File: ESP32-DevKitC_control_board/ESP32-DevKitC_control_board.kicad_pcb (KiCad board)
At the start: 2 copper layers, 100 x 100 mm, 35 parts, among them J1 Conn_01x03_Pin, J10 Conn_01x02_Pin, J11 Conn_01x02_Pin, J2 Conn_01x03_Pin, J3 Conn_01x02_Pin, J4 Conn_01x02_Pin, J5 Conn_01x04_Pin, J6 Conn_01x03_Pin, J7 Conn_01x03_Pin, J8 Conn_01x03_Pin, J9 Conn_01x03_Pin, U1 ESP32-DevKitC, U2 MCP2562-E-P

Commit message: ESP32基板　基板完成，ver 0.1
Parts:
- added D4: LED, LED_THT:LED_D5.0mm, F.Cu at (90.7, 33.0)
- added R12: 1k, Resistor_THT:R_Axial_DIN0207_L6.3mm_D2.5mm_P2.54mm_Vertical, F.Cu at (93.0, 24.4)
- C2: renamed from C1; footprint Capacitor_THT:C_Disc_D4.3mm_W1.9mm_P5.00mm -> Capacitor_THT:C_Disc_D5.0mm_W2.5mm_P2.50mm
- C3: renamed from C2; footprint Capacitor_THT:C_Disc_D4.3mm_W1.9mm_P5.00mm -> Capacitor_THT:C_Disc_D5.0mm_W2.5mm_P2.50mm
- J7: renamed from J5; footprint OU_connector:DF1EC-4P-2.5DSA -> OU_connector:DF1E-4P-2.5DS
- R1: footprint Resistor_THT:R_Axial_DIN0204_L3.6mm_D1.6mm_P5.08mm_Horizontal -> Resistor_THT:R_Axial_DIN0207_L6.3mm_D2.5mm_P2.54mm_Vertical
- moved J9 156.3 mm to (36.8, 68.8), turned to -90 degrees
- moved J5 152.9 mm to (48.3, 49.8), turned to 180 degrees
- moved C5 151.7 mm to (45.7, 71.6), turned to -90 degrees
- moved C3 150.5 mm to (49.5, 32.0), turned to 180 degrees
- moved J4 146.6 mm to (40.9, 44.7), turned to 90 degrees
- moved C2 145.8 mm to (53.1, 32.0)
- moved J7 141.6 mm to (40.9, 61.9), turned to 90 degrees
- moved U1 131.9 mm to (54.6, 42.9), turned to 180 degrees
- moved J6 128.5 mm to (40.9, 33.5), turned to 90 degrees
- moved R5 127.2 mm to (45.7, 68.8), turned to 90 degrees
- moved R9 126.4 mm to (41.4, 71.4), turned to 90 degrees
- moved R1 121.4 mm to (52.1, 49.8), turned to 90 degrees
- moved R2 120.1 mm to (47.5, 56.9), turned to 90 degrees
- moved R3 120.0 mm to (47.5, 62.2), turned to 90 degrees
- moved C1 115.7 mm to (87.9, 22.6), turned to -90 degrees
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- renumbered C7 to C1, C3 to C4, C4 to C5, C5 to C7, J10 to J1, J7 to J10, J6 to J11, J1 to J2, J2 to J3, J11 to J4, J3 to J5, J4 to J6, R22 to R10, R20 to R11, R14 to R2, R15 to R3, R17 to R4, R19 to R5, R23 to R6, R21 to R7, R16 to R8, R18 to R9, U2 to U1, U1 to U2
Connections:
- J3 pad 1: /PWM2 -> /PWM3
- J3 pad 3: /PWM3 -> /PWM2
- J7 pad 2: /GPIO27 -> /GPIO22
- J7 pad 4: /GPIO26 -> /GPIO21
- R2 pad 2: /GPIO26 -> /GPIO21
- R3 pad 2: /GPIO27 -> /GPIO22
- R9 pad 1: /GPIO14 -> /GPIO23
- U2 pad 10: /GPIO26 -> /PWM3
- U2 pad 11: /GPIO27 -> /PWM1
- U2 pad 12: /GPIO14 -> /PWM0
- U2 pad 30: /PWM1 -> /CAN_RX
- U2 pad 31: /PWM0 -> /CAN_TX
- U2 pad 33: /CAN_RX -> /GPIO21
- U2 pad 36: /CAN_TX -> /GPIO22
- U2 pad 37: /PWM2 -> /GPIO23
- U2 pad 9: /PWM3 -> /PWM2
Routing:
- net +3.3V: track 0.00 -> 230.4 mm
- net +5V: track 0.00 -> 67.0 mm
- net /GPIO4: track 0.00 -> 32.6 mm
- net /PWM3: track 0.00 -> 32.3 mm
- net /PWM0: track 0.00 -> 27.1 mm
- net /PWM1: track 0.00 -> 26.5 mm
- net /PWM2: track 0.00 -> 25.9 mm
- net /GPIO22: track 0.00 -> 25.6 mm
- net /CAN_RX: track 0.00 -> 25.1 mm
- net /GPIO33: track 0.00 -> 24.0 mm
- net /GPIO21: track 0.00 -> 23.4 mm, vias 0 -> 1
- net Net-(J8-Pin_1): track 0.00 -> 20.9 mm
- net /GPIO23: track 0.00 -> 20.7 mm
- net /GPIO32: track 0.00 -> 20.6 mm
- net /CAN_TX: track 0.00 -> 20.0 mm
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- added copper zone on B.Cu, net GND
- added copper zone on F.Cu, net GND
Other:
- board size 100 x 100 mm -> 85 x 60 mm
- board text added: "3.3V"
- board text added: "5V"
- board text added: "5V INPUT"
- board text added: "5V INPUTと USBを併用しない!"
- board text added: ":"
- board text added: "BoardID: TS26-CTRL-ESP32 ver 0.1"
- board text added: "CAN0"
- board text added: "GND"
- board text added: "GPIO13"
- board text added: "GPIO13,23, 32,33"
- board text added: "GPIO23"
- board text added: "GPIO32"
- board text added: "GPIO33"
- board text added: "GPIO4"
- board text added: "I2C"
- board text added: "IO"
- board text added: "Lp-C P-dn"
- board text added: "Lp-C ローパスフィルタ用C, P-dn もしくはプルダウン"
- board text added: "Lp-R"
- board text added: "Lp-R: ローパスフィルタ用R"
- board text added: "P-up"
- board text added: "P-up: プルアップ"
- board text added: "PW0,2"
- board text added: "PW1,3"
- board text added: "PWM0,1"
- board text added: "PWM2,3"
- board text added: "Pull-up Resistor"
- board text added: "SCL"
- board text added: "SDA"
- board text added: "Serial Servo"
- board text added: "ローパスフィルタ未使用時 Lp-Rは0Ωに"
- board text added: "岡山大学 ロボット研究会"
- board text added: "終端抵抗 有効化"

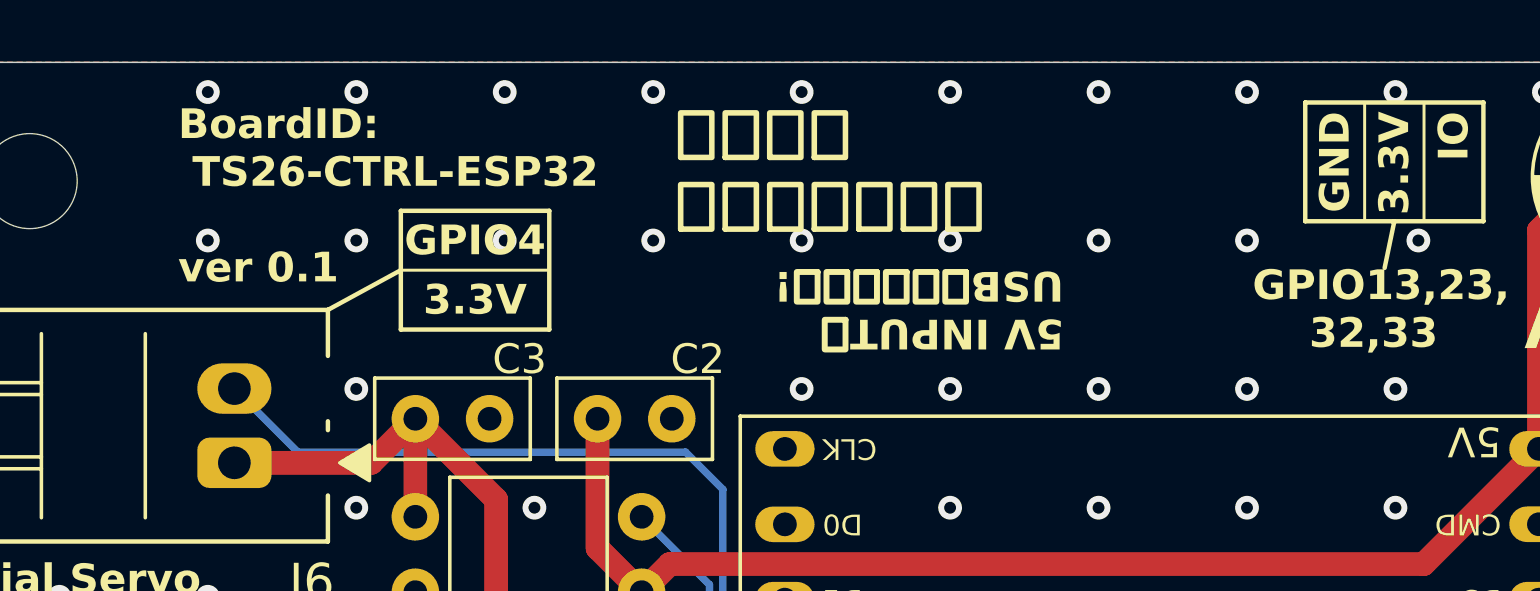
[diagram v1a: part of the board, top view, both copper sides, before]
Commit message: ESP32基板　不足していたシルクを追加
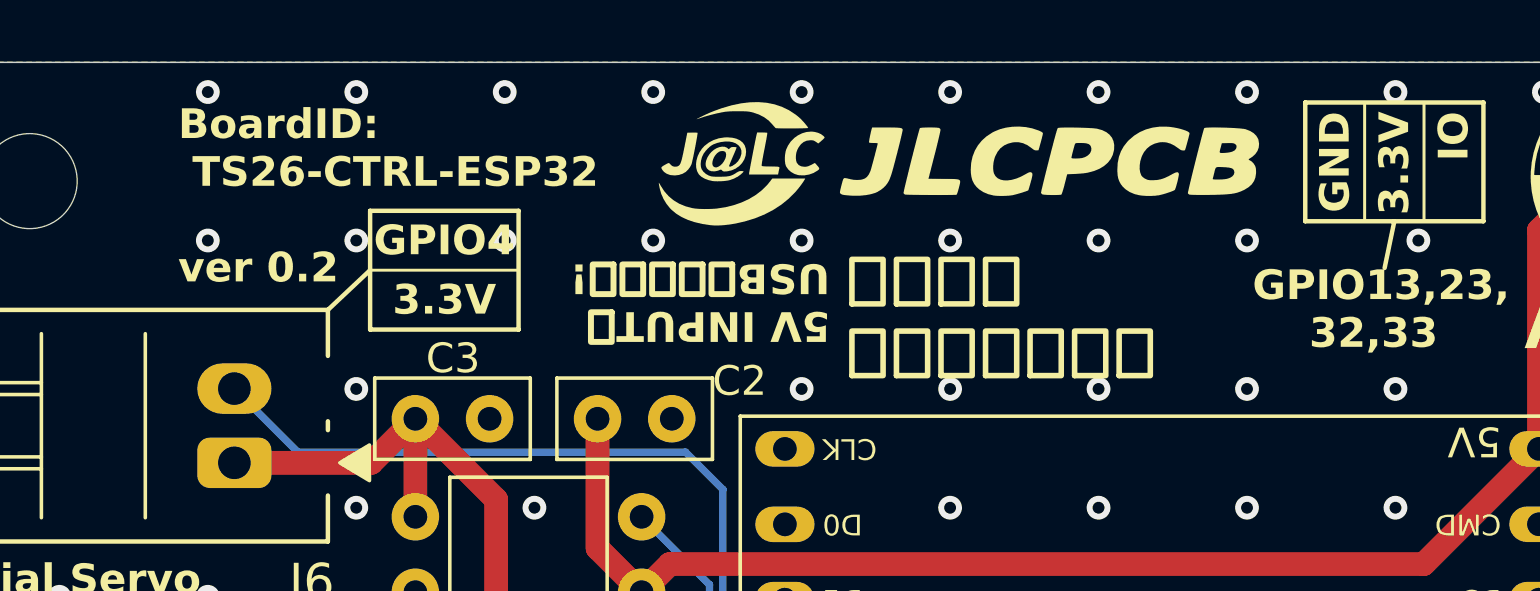
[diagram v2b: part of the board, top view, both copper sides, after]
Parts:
- added G***: LOGO, OU_Picture:JLCPCB_Logo_4x20, F.Cu at (65.3, 23.4)
- added G***: LOGO, OU_Picture:OkaLogo, B.Cu at (72.6, 34.3)
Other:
- board text added: "2026/10/02 Designed by E.Yoshioka"
- board text added: "5V INPUTと USBの併用ダメ!"
- board text added: "BoardID: TS26-CTRL-ESP32 ver 0.2"
- board text added: "No."
- board text removed: "5V INPUTと USBを併用しない!"
- board text removed: "BoardID: TS26-CTRL-ESP32 ver 0.1"

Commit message: ESP32基板　CAN0をCAN1に改名，ver 0.3 STMの場合，CANの通し番号は1からっぽい．
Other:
- board text added: "BoardID: TS26-CTRL-ESP32 ver 0.3"
- board text added: "CAN1"
- board text removed: "BoardID: TS26-CTRL-ESP32 ver 0.2"
- board text removed: "CAN0"
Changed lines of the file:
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@@
 		)
 	)
-	(gr_text "BoardID:\n TS26-CTRL-ESP32\n\nver 0.2"
+	(gr_text "BoardID:\n TS26-CTRL-ESP32\n\nver 0.3"
 		(at 39 24.5 0)
 		(layer "F.SilkS")
@@
 		)
 	)
-	(gr_text "CAN0"
+	(gr_text "CAN1"
 		(at 30.4 49.2 0)
 		(layer "F.SilkS" knockout)

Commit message: ESP32基板　I2C部分のネットラベル名を変更
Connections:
- net /CAN0+ renamed /CAN1+
- net /CAN0- renamed /CAN1-
- net /GPIO21 renamed /I2C_SDA
- net /GPIO22 renamed /I2C_SCL
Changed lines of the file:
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@@
 			(layers "*.Cu" "*.Mask")
 			(remove_unused_layers no)
-			(net "/GPIO21")
+			(net "/I2C_SDA")
 			(pinfunction "GPIO21_33")
 			(pintype "bidirectional")
@@
 			(layers "*.Cu" "*.Mask")
 			(remove_unused_layers no)
-			(net "/GPIO22")
+			(net "/I2C_SCL")
 			(pinfunction "GPIO22_36")
 			(pintype "bidirectional")
@@
 			(layers "*.Cu" "*.Mask")
 			(remove_unused_layers no)
-			(net "/GPIO22")
+			(net "/I2C_SCL")
 			(pinfunction "Pin_2_2")
 			(pintype "passive")
@@
 			(layers "*.Cu" "*.Mask")
 			(remove_unused_layers no)
-			(net "/GPIO21")
+			(net "/I2C_SDA")
 			(pinfunction "Pin_4_4")
 			(pintype "passive")
@@
 			(remove_unused_layers no)
 			(roundrect_rratio 0.25)
-			(net "/CAN0+")
+			(net "/CAN1+")
 			(pinfunction "Pin_1_1")
 			(pintype "passive")
@@
 			(layers "*.Cu" "*.Mask")
 			(remove_unused_layers no)
-			(net "/CAN0-")
+			(net "/CAN1-")
 			(pinfunction "Pin_2_2")
 			(pintype "passive")
@@
 			(layers "*.Cu" "*.Mask")
 			(remove_unused_layers no)
-			(net "/GPIO22")
+			(net "/I2C_SCL")
 			(pintype "passive")
 		)
@@
 			(layers "*.Cu" "*.Mask")
 			(remove_unused_layers no)
-			(net "/CAN0+")
+			(net "/CAN1+")
 			(pinfunction "Pin_2_2")
 			(pintype "passive")
@@
 			(layers "*.Cu" "*.Mask")
 			(remove_unused_layers no)
-			(net "/GPIO21")
+			(net "/I2C_SDA")
 			(pintype "passive")
 		)
@@
 			(layers "*.Cu" "*.Mask")
 			(remove_unused_layers no)
-			(net "/CAN0-")
+			(net "/CAN1-")
 			(pintype "passive")
 		)
@@
 			(layers "*.Cu" "*.Mask")
 			(remove_unused_layers no)
-			(net "/CAN0-")
+			(net "/CAN1-")
 			(pinfunction "CANL_6")
 			(pintype "bidirectional")
@@
 			(layers "*.Cu" "*.Mask")
 			(remove_unused_layers no)
-			(net "/CAN0+")
+			(net "/CAN1+")
 			(pinfunction "CANH_7")
 			(pintype "bidirectional")
@@
 		(net "/CAN_TX")
 	)
-	(via
-		(at 47.498 54.356)
-		(size 0.6)
-		(drill 0.3)
-		(layers "F.Cu" "B.Cu")
-		(net "/GPIO21")
-	)
-	(segment
-		(start 59.43232 66.03728)
-		(end 59.17928 66.03728)
-		(width 0.25)
-		(layer "B.Cu")
-		(net "/GPIO21")
-	)
-	(segment
-		(start 47.458 54.396)
-		(end 47.498 54.356)
-		(width 0.25)
-		(layer "B.Cu")
-		(net "/GPIO21")
-	)
-	(segment
-		(start 40.894 54.396)
-		(end 47.458 54.396)
-		(width 0.25)
-		(layer "B.Cu")
-		(net "/GPIO21")
-	)
-	(segment
-		(start 59.17928 66.03728)
-		(end 47.498 54.356)
-		(width 0.25)
-		(layer "B.Cu")
-		(net "/GPIO21")
-	)
-	(segment
-		(start 47.204 59.396)
-		(end 47.498 59.69)
-		(width 0.25)
-		(layer "B.Cu")
-		(net "/GPIO22")
-	)
-	(segment
-		(start 58.10732 72.33228)
-		(end 58.10732 70.29932)
-		(width 0.25)
-		(layer "B.Cu")
-		(net "/GPIO22")
-	)
-	(segment
-		(start 59.43232 73.65728)
-		(end 58.10732 72.33228)
-		(width 0.25)
-		(layer "B.Cu")
-		(net "/GPIO22")
-	)
-	(segment
-		(start 58.10732 70.29932)
-		(end 47.498 59.69)
-		(width 0.25)
-		(layer "B.Cu")
-		(net "/GPIO22")
-	)
-	(segment
-		(start 40.894 59.396)
-		(end 47.204 59.396)
-		(width 0.25)
-		(layer "B.Cu")
-		(net "/GPIO22")
-	)
 	(segment
 		(start 41.402 72.50537)
@@
 	)
 	(segment
+		(start 36.83 68.834)
+		(end 41.402 68.834)
+		(width 0.25)
+		(layer "B.Cu")
+		(net "Net-(J9-Pin_1)")
+	)
+	(segment
+		(start 45.72 71.628)
+		(end 45.72 68.834)
+		(width 0.25)
+		(layer "B.Cu")
+		(net "Net-(J9-Pin_1)")
+	)
+	(segment
+		(start 41.402 68.834)
+		(end 45.72 68.834)
+		(width 0.25)
+		(layer "B.Cu")
+		(net "Net-(J9-Pin_1)")
+	)
+	(segment
+		(start 48.26 49.784)
+		(end 52.07 49.784)
+		(width 0.25)
+		(layer "B.Cu")
+		(net "Net-(J5-Pin_1)")
+	)
+	(segment
 		(start 48.26 41.656)
 		(end 46.99 40.386)
 		(width 0.25)
 		(layer "B.Cu")
-		(net "/CAN0+")
+		(net "/CAN1+")
 	)
 	(segment
@@
 		(width 0.25)
 		(layer "B.Cu")
-		(net "/CAN0+")
+		(net "/CAN1+")
 	)
 	(segment
@@
 		(width 0.25)
 		(layer "B.Cu")
-		(net "/CAN0+")
+		(net "/CAN1+")
 	)
 	(segment
@@
 		(width 0.25)
 		(layer "B.Cu")
-		(net "/CAN0+")
+		(net "/CAN1+")
 	)
 	(segment
@@
 		(width 0.25)
 		(layer "B.Cu")
-		(net "/CAN0-")
+		(net "/CAN1-")
 	)
 	(segment
@@
 		(width 0.25)
 		(layer "B.Cu")
-		(net "/CAN0-")
+		(net "/CAN1-")
 	)
 	(segment
@@
 		(width 0.25)
 		(layer "B.Cu")
-		(net "/CAN0-")
+		(net "/CAN1-")
 	)
 	(segment
@@
 		(width 0.25)
 		(layer "B.Cu")
-		(net "/CAN0-")
+		(net "/CAN1-")
 	)
 	(segment
@@
 		(width 0.25)
 		(layer "B.Cu")
-		(net "/CAN0-")
+		(net "/CAN1-")
+	)
+	(via
+		(at 47.498 54.356)
+		(size 0.6)
+		(drill 0.3)
+		(layers "F.Cu" "B.Cu")
+		(net "/I2C_SDA")
 	)
 	(segment
-		(start 36.83 68.834)
-		(end 41.402 68.834)
+		(start 59.43232 66.03728)
+		(end 59.17928 66.03728)
 		(width 0.25)
 		(layer "B.Cu")
-		(net "Net-(J9-Pin_1)")
+		(net "/I2C_SDA")
 	)
 	(segment
-		(start 45.72 71.628)
-		(end 45.72 68.834)
+		(start 47.458 54.396)
+		(end 47.498 54.356)
 		(width 0.25)
 		(layer "B.Cu")
-		(net "Net-(J9-Pin_1)")
+		(net "/I2C_SDA")
 	)
 	(segment
-		(start 41.402 68.834)
-		(end 45.72 68.834)
+		(start 40.894 54.396)
+		(end 47.458 54.396)
 		(width 0.25)
 		(layer "B.Cu")
-		(net "Net-(J9-Pin_1)")
+		(net "/I2C_SDA")
 	)
 	(segment
-		(start 48.26 49.784)
-		(end 52.07 49.784)
+		(start 59.17928 66.03728)
+		(end 47.498 54.356)
 		(width 0.25)
 		(layer "B.Cu")
-		(net "Net-(J5-Pin_1)")
+		(net "/I2C_SDA")
+	)
+	(segment
+		(start 47.204 59.396)
+		(end 47.498 59.69)
+		(width 0.25)
+		(layer "B.Cu")
+		(net "/I2C_SCL")
+	)
+	(segment
+		(start 58.10732 72.33228)
+		(end 58.10732 70.29932)
+		(width 0.25)
+		(layer "B.Cu")
+		(net "/I2C_SCL")
+	)
+	(segment
+		(start 59.43232 73.65728)
+		(end 58.10732 72.33228)
+		(width 0.25)
+		(layer "B.Cu")
+		(net "/I2C_SCL")
+	)
+	(segment
+		(start 58.10732 70.29932)
+		(end 47.498 59.69)
+		(width 0.25)
+		(layer "B.Cu")
+		(net "/I2C_SCL")
+	)
+	(segment
+		(start 40.894 59.396)
+		(end 47.204 59.396)
+		(width 0.25)
+		(layer "B.Cu")
+		(net "/I2C_SCL")
 	)
 	(zone
